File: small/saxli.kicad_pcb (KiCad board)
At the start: 4 copper layers, 160.5 x 102.4 mm, 195 parts, among them IC1 PIC32MX350F256H-V_PT, IC2 SIM808, J1 78800-0001, J10 Conn_01x06_Female, J11 Conn_Coaxial, J12 Conn_Coaxial, J2 Screw_Terminal_01x02, J3 Micro_SD_Card, J4 Conn_01x05_Female, J5 Conn_02x04_Odd_Even, J6 RJ45_Amphenol_RJMG1BD3B8K1ANR, J7 Screw_Terminal_01x08, J8 Screw_Terminal_01x08, J9 Screw_Terminal_01x08, Q1 2N7002, Q2 2N7002, Q3 2N7002, U1 LM358, U10 TPS5430DDAR, U11 EL357N(C)(TA)-G, U12 EL357N(C)(TA)-G, U13 ASSR-1218, U14 ST485EBDR, U15 ASSR-1218, U16 SRV05-4, U18 ULN2003A, U2 LM7805_TO220, U20 TPS5430DDAR, U4 ENC28J60x-SS, U5 AT25M02, U6 EL357N(C)(TA)-G, U7 EL357N(C)(TA)-G, U8 PCF8563T, U9 ISO1540, Y1 Crystal, Y2 Crystal

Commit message: power supply ldo changes
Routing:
- net GND: track 1177.6 -> 1203.8 mm, vias 65 -> 85
- net VDD5: track 333.4 -> 342.8 mm, vias 9 -> 10
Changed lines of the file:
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@@
     (thickness 1.6)
     (drawings 7)
-    (tracks 2387)
+    (tracks 2435)
     (zones 0)
     (modules 195)
@@
   )
   (setup
-    (last_trace_width 0.25)
+    (last_trace_width 1.5)
     (user_trace_width 0.5)
     (user_trace_width 1)
@@
   (segment (start 43.366 101.913) (end 43.18 101.727) (width 1) (layer F.Cu) (net 1))
   (segment (start 43.18 101.727) (end 43.18 95.25) (width 1) (layer F.Cu) (net 1))
-  (segment (start 68.14 102.811) (end 73.406 102.811) (width 0.5) (layer F.Cu) (net 1))
   (segment (start 68.072 98.311) (end 68.072 102.743) (width 0.5) (layer F.Cu) (net 1))
   (segment (start 68.072 102.743) (end 68.14 102.811) (width 0.5) (layer F.Cu) (net 1))
   (segment (start 68.072 98.311) (end 65.913 98.311) (width 0.5) (layer F.Cu) (net 1))
-  (segment (start 65.278 101.854) (end 62.103 101.854) (width 0.5) (layer F.Cu) (net 1))
+  (segment (start 65.278 101.854) (end 64.643 101.854) (width 0.5) (layer F.Cu) (net 1))
   (segment (start 65.913 98.311) (end 65.913 101.219) (width 0.5) (layer F.Cu) (net 1))
   (segment (start 65.913 101.219) (end 65.278 101.854) (width 0.5) (layer F.Cu) (net 1))
@@
   (segment (start 125.476 47.371) (end 125.997 47.892) (width 0.5) (layer F.Cu) (net 1))
   (segment (start 103.378 47.957) (end 103.378 46.765) (width 0.25) (layer F.Cu) (net 1))
+  (segment (start 72.449 101.854) (end 73.406 102.811) (width 1.5) (layer F.Cu) (net 1))
+  (segment (start 62.103 101.854) (end 62.738 101.854) (width 1.5) (layer F.Cu) (net 1))
+  (segment (start 62.103 101.854) (end 62.103 101.854) (width 0.5) (layer F.Cu) (net 1))
+  (via (at 62.103 101.854) (size 0.5) (drill 0.3) (layers F.Cu B.Cu) (net 1))
+  (segment (start 62.738 101.854) (end 63.373 101.854) (width 1.5) (layer F.Cu) (net 1))
+  (via (at 62.738 101.854) (size 0.5) (drill 0.3) (layers F.Cu B.Cu) (net 1))
+  (segment (start 63.373 101.854) (end 64.008 101.854) (width 1.5) (layer F.Cu) (net 1))
+  (via (at 63.373 101.854) (size 0.5) (drill 0.3) (layers F.Cu B.Cu) (net 1))
+  (segment (start 64.008 101.854) (end 65.913 101.854) (width 1.5) (layer F.Cu) (net 1))
+  (via (at 64.008 101.854) (size 0.5) (drill 0.3) (layers F.Cu B.Cu) (net 1))
+  (segment (start 64.643 101.854) (end 62.103 101.854) (width 0.5) (layer F.Cu) (net 1))
+  (via (at 64.643 101.854) (size 0.5) (drill 0.3) (layers F.Cu B.Cu) (net 1))
+  (segment (start 65.278 101.854) (end 65.278 101.854) (width 0.5) (layer F.Cu) (net 1))
+  (via (at 65.278 101.854) (size 0.5) (drill 0.3) (layers F.Cu B.Cu) (net 1))
+  (segment (start 65.913 101.854) (end 66.548 101.854) (width 1.5) (layer F.Cu) (net 1))
+  (via (at 65.913 101.854) (size 0.5) (drill 0.3) (layers F.Cu B.Cu) (net 1))
+  (segment (start 66.548 101.854) (end 67.183 101.854) (width 1.5) (layer F.Cu) (net 1))
+  (via (at 66.548 101.854) (size 0.5) (drill 0.3) (layers F.Cu B.Cu) (net 1))
+  (segment (start 67.183 101.854) (end 67.818 101.854) (width 1.5) (layer F.Cu) (net 1))
+  (via (at 67.183 101.854) (size 0.5) (drill 0.3) (layers F.Cu B.Cu) (net 1))
+  (segment (start 67.818 101.854) (end 72.449 101.854) (width 1.5) (layer F.Cu) (net 1))
+  (via (at 67.818 101.854) (size 0.5) (drill 0.3) (layers F.Cu B.Cu) (net 1))
+  (segment (start 69.02 102.811) (end 67.75 102.811) (width 1.5) (layer F.Cu) (net 1))
+  (segment (start 68.14 102.811) (end 69.02 102.811) (width 0.5) (layer F.Cu) (net 1))
+  (segment (start 61.781 102.811) (end 62.67 102.811) (width 1.5) (layer F.Cu) (net 1))
+  (segment (start 62.035 102.811) (end 61.781 102.811) (width 1.5) (layer F.Cu) (net 1))
+  (via (at 62.035 102.811) (size 0.5) (drill 0.3) (layers F.Cu B.Cu) (net 1))
+  (segment (start 62.67 102.811) (end 63.305 102.811) (width 1.5) (layer F.Cu) (net 1))
+  (via (at 62.67 102.811) (size 0.5) (drill 0.3) (layers F.Cu B.Cu) (net 1))
+  (segment (start 63.305 102.811) (end 63.94 102.811) (width 1.5) (layer F.Cu) (net 1))
+  (via (at 63.305 102.811) (size 0.5) (drill 0.3) (layers F.Cu B.Cu) (net 1))
+  (segment (start 63.94 102.811) (end 64.575 102.811) (width 1.5) (layer F.Cu) (net 1))
+  (via (at 63.94 102.811) (size 0.5) (drill 0.3) (layers F.Cu B.Cu) (net 1))
+  (segment (start 64.575 102.811) (end 65.21 102.811) (width 1.5) (layer F.Cu) (net 1))
+  (via (at 64.575 102.811) (size 0.5) (drill 0.3) (layers F.Cu B.Cu) (net 1))
+  (segment (start 65.21 102.811) (end 65.845 102.811) (width 1.5) (layer F.Cu) (net 1))
+  (via (at 65.21 102.811) (size 0.5) (drill 0.3) (layers F.Cu B.Cu) (net 1))
+  (segment (start 65.845 102.811) (end 66.48 102.811) (width 1.5) (layer F.Cu) (net 1))
+  (via (at 65.845 102.811) (size 0.5) (drill 0.3) (layers F.Cu B.Cu) (net 1))
+  (segment (start 66.48 102.811) (end 67.115 102.811) (width 1.5) (layer F.Cu) (net 1))
+  (via (at 66.48 102.811) (size 0.5) (drill 0.3) (layers F.Cu B.Cu) (net 1))
+  (segment (start 67.115 102.811) (end 73.406 102.811) (width 1.5) (layer F.Cu) (net 1))
+  (via (at 67.115 102.811) (size 0.5) (drill 0.3) (layers F.Cu B.Cu) (net 1))
+  (segment (start 67.75 102.811) (end 62.035 102.811) (width 1.5) (layer F.Cu) (net 1))
+  (via (at 67.75 102.811) (size 0.5) (drill 0.3) (layers F.Cu B.Cu) (net 1))
   (segment (start 57.912 84.025) (end 58.977 84.025) (width 0.5) (layer F.Cu) (net 2))
   (segment (start 58.977 84.025) (end 59.817 83.185) (width 0.5) (layer F.Cu) (net 2))
@@
   (segment (start 96.3695 51.1575) (end 95.6545 51.1575) (width 0.25) (layer F.Cu) (net 57))
   (segment (start 129.921 51.1575) (end 96.3695 51.1575) (width 0.25) (layer F.Cu) (net 57))
+  (segment (start 62.846 96.511) (end 62.103 97.254) (width 1.5) (layer F.Cu) (net 57))
+  (segment (start 71.126 96.511) (end 62.846 96.511) (width 1.5) (layer F.Cu) (net 57))
+  (segment (start 69.482 96.761) (end 69.482 96.761) (width 1.5) (layer B.Cu) (net 57))
+  (via (at 69.482 96.761) (size 1) (drill 0.6) (layers F.Cu B.Cu) (net 57))
   (segment (start 175.188012 79.11901) (end 173.86101 79.11901) (width 0.25) (layer F.Cu) (net 58))
   (segment (start 175.388002 79.319) (end 175.188012 79.11901) (width 0.25) (layer F.Cu) (net 58))

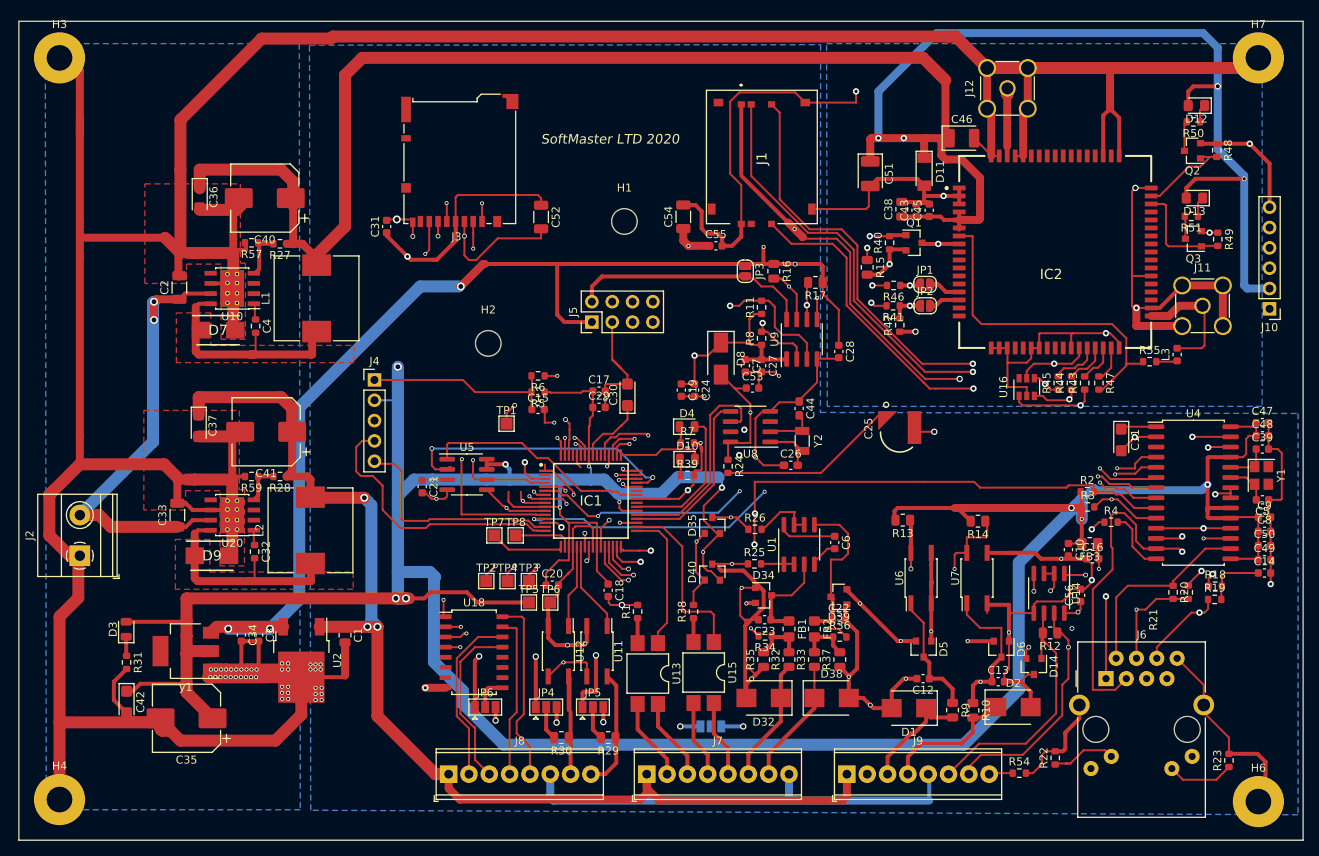
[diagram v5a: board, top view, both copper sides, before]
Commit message: Isolated DCDC added
power LED added
reverse voltage protection added
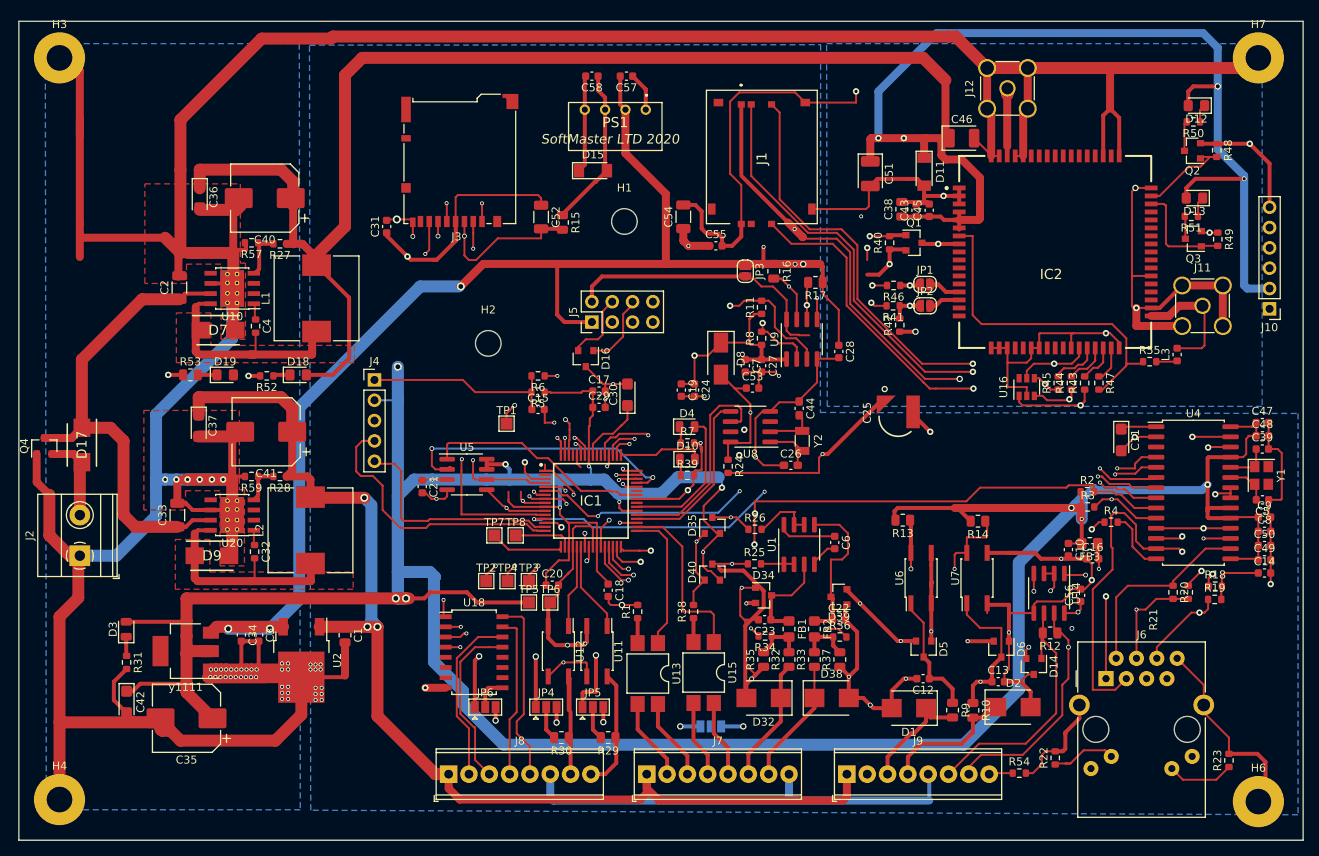
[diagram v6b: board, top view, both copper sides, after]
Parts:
- added C57: 0.1u, Capacitor_SMD:C_0603_1608Metric, F.Cu at (114.0, 27.7)
- added C58: 0.1u, Capacitor_SMD:C_0603_1608Metric, F.Cu at (109.7, 27.7)
- added D15: D_Zener, Diode_SMD:D_MiniMELF, F.Cu at (109.9, 39.5)
- added D16: PSM712-LF-T7, Package_TO_SOT_SMD:SOT-23, F.Cu at (109.0, 63.0)
- added D17: SS34B-HF, mylib:DIOM5336X320N, F.Cu at (46.0, 73.8)
- added D18: LED, LED_SMD:LED_0805_2012Metric_Pad1.15x1.40mm_HandSolder, F.Cu at (73.0, 65.0)
- added D19: LED, LED_SMD:LED_0805_2012Metric_Pad1.15x1.40mm_HandSolder, F.Cu at (63.9, 65.0)
- added PS1: TEA_1-0505, small:TEA10505, F.Cu at (116.5, 31.9)
- added Q4: AO3401A, Package_TO_SOT_SMD:SOT-23, F.Cu at (41.3, 73.9)
- added R52: 200, Resistor_SMD:R_0603_1608Metric, F.Cu at (69.1, 65.2)
- added R53: 1k, Resistor_SMD:R_0805_2012Metric, F.Cu at (59.5, 65.0)
- moved R15 38.5 mm to (106.0, 46.0)
- moved C25 1.97 mm to (148.0, 70.3)
- renumbered у1 to у1111
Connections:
- net /communication/GND_ISO renamed GND_IS
- net /communication/VDD_ISO renamed 5V_IS
- J2 pad 2: 24Vin -> Net-(D17-Pad2)
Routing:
- net VDD5: track 342.8 -> 412.7 mm, vias 10 -> 11
- net GND_IS: track 48.4 -> 94.8 mm
- net 5V_IS: track 30.5 -> 71.6 mm
- net POWER_SIM: track 280.5 -> 300.1 mm
- net GND: track 1203.8 -> 1220.3 mm, vias 85 -> 95
- net Net-(D17-Pad2): track 0.00 -> 10.9 mm
- net /communication/SCL_ISO: track 28.4 -> 37.7 mm
- net /communication/SDA_ISO: track 30.9 -> 39.7 mm
- net 24Vin: track 57.6 -> 60.3 mm, vias 2 -> 0
- net U3TXSIM800: track 67.2 -> 64.7 mm
- net Net-(D19-Pad1): track 0.00 -> 2.41 mm
- net Net-(D18-Pad1): track 0.00 -> 2.13 mm
- net U3RXSIM800: track 75.3 -> 73.2 mm
- net ENC_SS: track 87.9 -> 85.8 mm
- net BATTERY: track 22.3 -> 24.2 mm, vias 0 -> 1

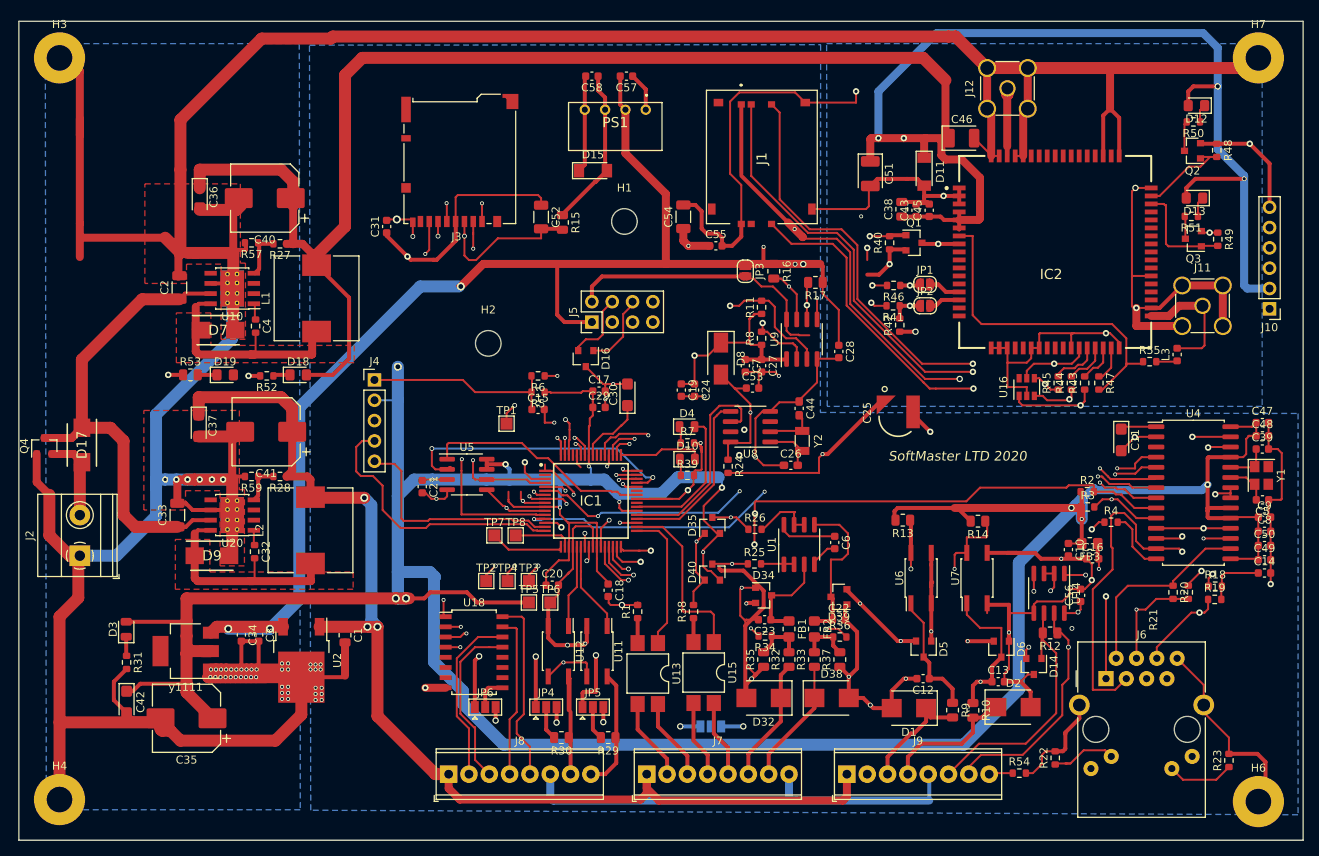
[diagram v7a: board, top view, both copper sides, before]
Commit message: working on JLCPCB orientations
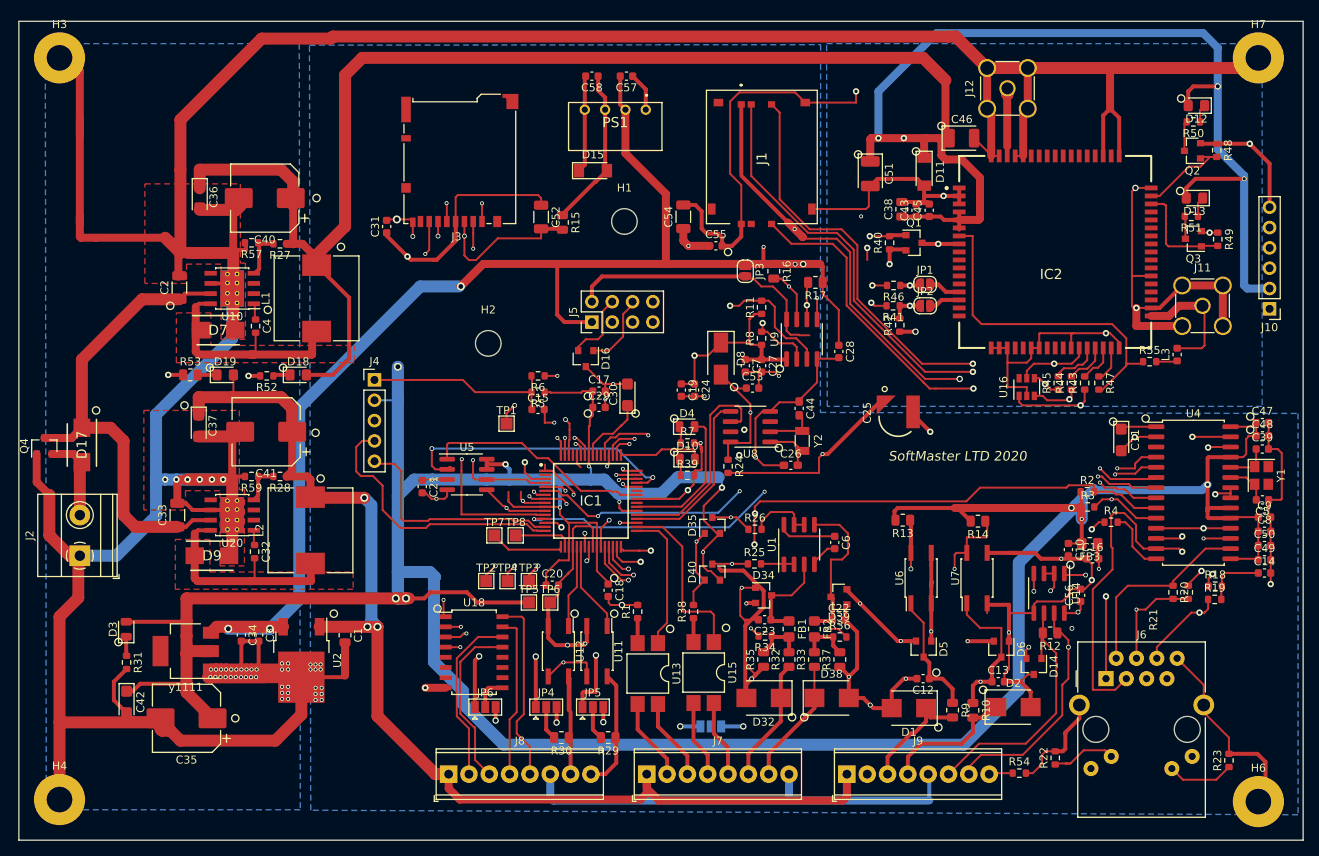
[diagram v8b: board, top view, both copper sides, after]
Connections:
- D19 pad 2: Net-(D19-Pad2) -> 12V
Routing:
- net 12V: track 218.6 -> 221.4 mm
- net GND: track 1220.3 -> 1217.8 mm
